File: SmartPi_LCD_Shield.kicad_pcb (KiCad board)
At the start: 2 copper layers, 84 x 58 mm, 47 parts, among them J1 Ant_SMA, J3 Micro_SD_Card, J4 Conn_01x02, J5 Conn_01x16, Q1 BC547, SW1 Reset, SW2 UP, SW3 LEFT, SW4 RIGHT, SW5 SELECT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

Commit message: finished routing
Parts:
- added CreativeCommonsPublicDomain1: License, Symbol:Symbol_CreativeCommonsPublicDomain_SilkScreenTop_Small, B.Cu at (182.9, 123.8)
- added J2: Conn_01x01, Connector_PinSocket_2.54mm:PinSocket_1x01_P2.54mm_Vertical, F.Cu at (225.4, 127.0)
- added KiCad1: License, Symbol:KiCad-Logo2_8mm_SilkScreen, B.Cu at (184.8, 113.7)
- added RV2: 10k, Potentiometer_THT:Potentiometer_Bourns_3296X_Horizontal, F.Cu at (153.0, 98.4)
- JP6: moved to F.Cu
- LOGO1: footprint Symbol:OSHW-Logo2_7.3x6mm_SilkScreen -> Symbol:OSHW-Logo2_14.6x12mm_SilkScreen; moved to B.Cu
- moved LOGO1 88.6 mm to (170.8, 112.4)
- moved JP6 57.8 mm to (221.0, 97.8), turned to 270 degrees
- moved JP14 43.0 mm to (208.3, 140.3), turned to 180 degrees
- moved JP1 27.1 mm to (171.4, 97.8), turned to 90 degrees
- moved TP4 4.84 mm to (210.2, 132.1)
- moved TP2 4.62 mm to (218.4, 132.1)
- moved TP5 4.49 mm to (213.4, 132.1)
- moved TP3 4.44 mm to (221.6, 132.1)
- moved J3 2.54 mm to (219.7, 113.7)
- moved JP10 2.54 mm to (165.1, 131.4)
- moved JP11 2.54 mm to (162.6, 131.4)
- moved JP9 2.54 mm to (167.6, 131.4)
- moved TP6 2.54 mm to (200.0, 120.7)
- moved TP1 2.29 mm to (219.7, 107.3)
- moved RV1 1.91 mm to (153.0, 93.3)
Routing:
- net Net-(JP6-Pad2): track 3.16 -> 132.8 mm
- net Net-(BT1-Pad1): track 0.00 -> 110.9 mm
- net +5V: track 57.8 -> 143.9 mm
- net /SCL: track 63.4 -> 134.9 mm
- net /SDA: track 68.2 -> 136.2 mm
- net +3V3: track 96.7 -> 163.6 mm
- net Net-(JP12-Pad2): track 12.1 -> 77.7 mm
- net /RFM_D0: track 3.16 -> 64.2 mm
- net /CLK: track 9.26 -> 56.9 mm
- net /Key0: track 37.7 -> 46.1 mm
- net /RW: track 25.1 -> 32.3 mm
- net GND: track 0.00 -> 6.99 mm, vias 0 -> 55
- net /MISO: track 41.7 -> 48.0 mm
- net /SS2: track 34.0 -> 28.0 mm
- net Net-(A1-Pad3): track 124.4 -> 129.4 mm
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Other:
- net class PWR added: clearance 0, trace_width 0.5, via_dia 0.8, via_drill 0.4
- net class sat added: clearance 0.5, trace_width 1, via_dia 0.8, via_drill 0.4
- board text added: "SmartPi LCD Shield"
- board text added: "https://github.com/nerdyscout/SmartPi_LCD_Shield"

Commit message: added hexbuffer for sd card
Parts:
- added TP7: TestPoint, TestPoint:TestPoint_Pad_D1.5mm, F.Cu at (256.5, 109.2)
- added TP8: TestPoint, TestPoint:TestPoint_Pad_D1.5mm, F.Cu at (254.6, 105.4)
- added U4: 4050, Package_SO:SOIC-16_3.9x9.9mm_P1.27mm, F.Cu at (208.3, 127.0)
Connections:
- BZ1 pad 1: +5V -> (no net)
- J3 pad 2: /SS3 -> Net-(J3-Pad2)
- J3 pad 5: /CLK -> Net-(J3-Pad5)
- J3 pad 7: /MISO -> Net-(J3-Pad7)
- JP10 pad 3: +3V3 -> +5V
- JP11 pad 3: +3V3 -> +5V
- JP9 pad 3: +3V3 -> +5V
- R1 pad 2: +3V3 -> +5V
- R2 pad 2: +3V3 -> +5V
- R3 pad 2: +3V3 -> +5V
- R4 pad 2: +3V3 -> +5V
- U2 pad 18: +3V3 -> +5V
- U2 pad 9: +3V3 -> +5V
- U3 pad 2: +3V3 -> +5V
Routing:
- net /SS3: track 50.6 -> 0.00 mm
- net /MOSI: track 47.4 -> 28.4 mm, vias 1 -> 0
- net /MISO: track 48.0 -> 29.4 mm, vias 1 -> 0
- net /CLK: track 56.9 -> 39.3 mm, vias 1 -> 0
- net GND: vias 55 -> 54
- net /SCL: vias 0 -> 1

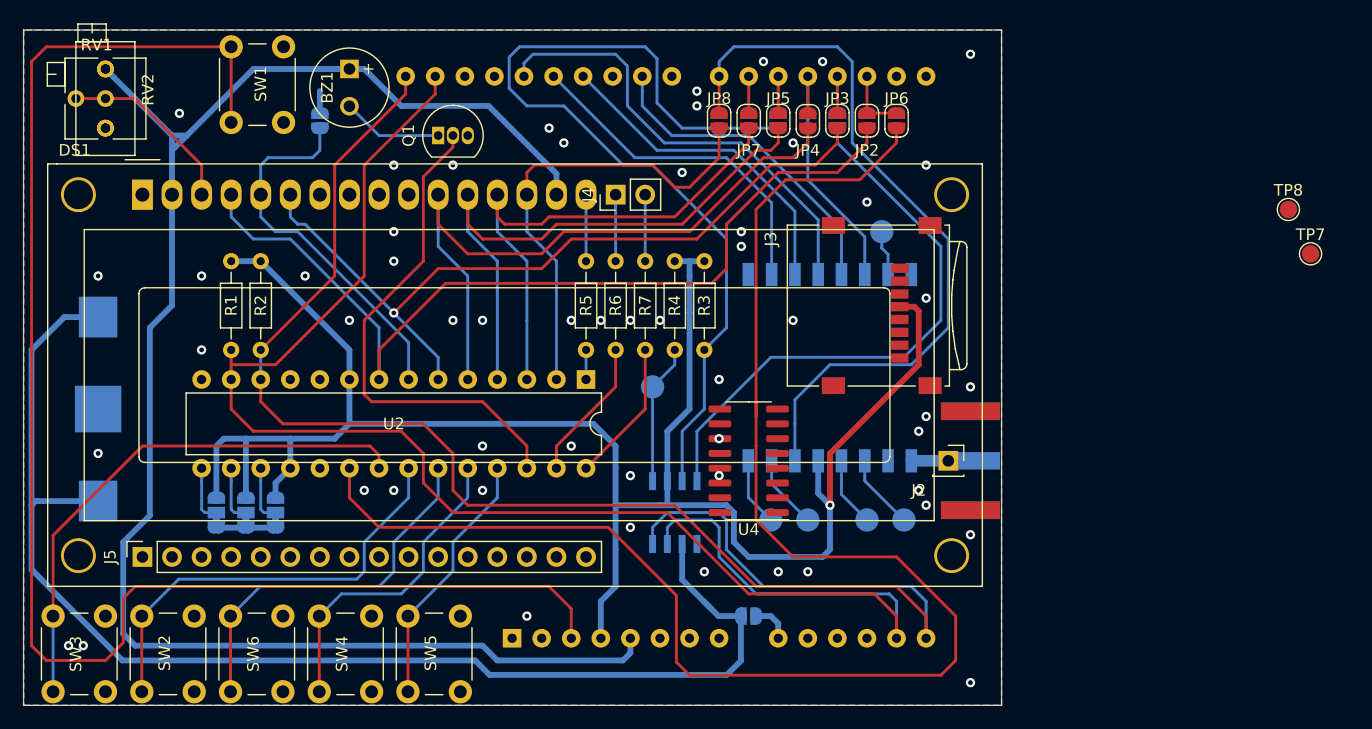
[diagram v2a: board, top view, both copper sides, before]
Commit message: routing complete with hex buffer
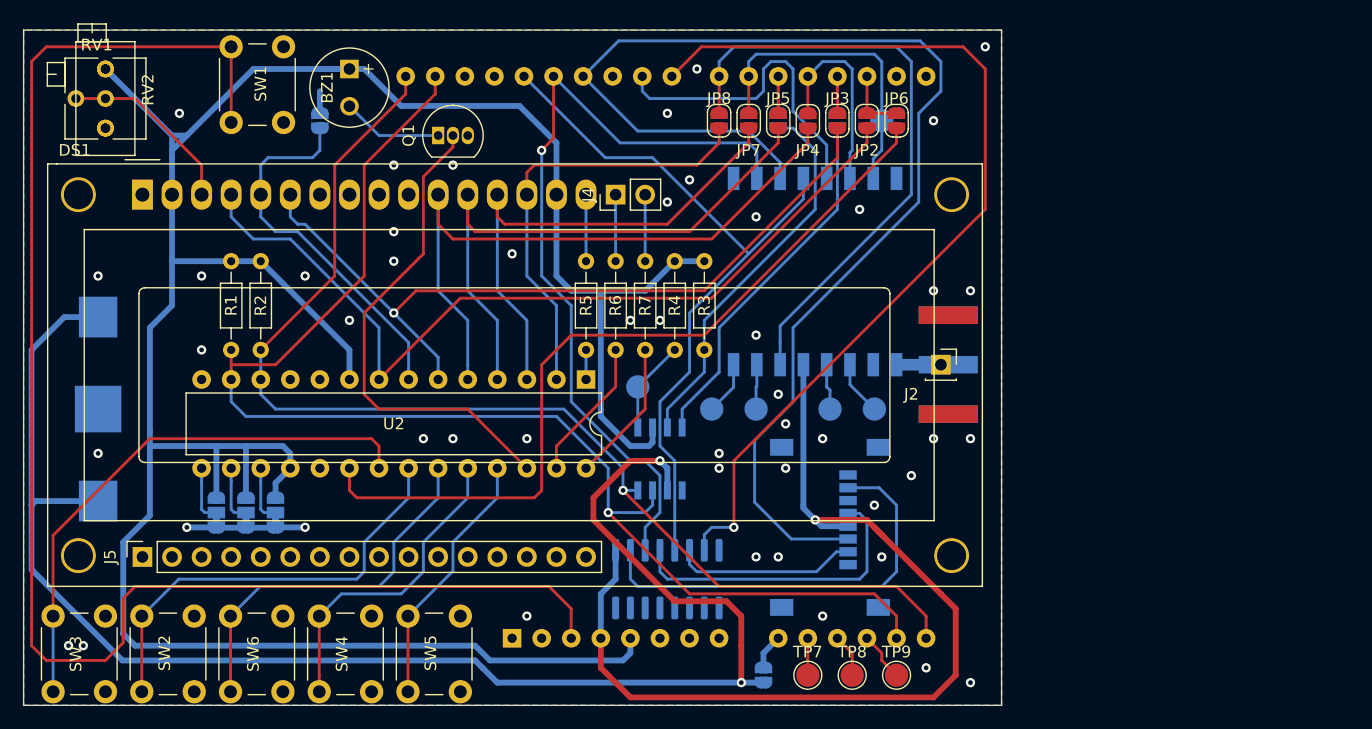
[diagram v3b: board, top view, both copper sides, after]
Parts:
- removed CreativeCommonsPublicDomain1: License, Symbol:Symbol_CreativeCommonsPublicDomain_SilkScreenTop_Small
- added TP9: TestPoint, TestPoint:TestPoint_Pad_D2.0mm, F.Cu at (221.0, 145.4)
- J3, U4: moved to B.Cu
- TP7, TP8: footprint TestPoint:TestPoint_Pad_D1.5mm -> TestPoint:TestPoint_Pad_D2.0mm
- moved TP7 56.3 mm to (213.4, 145.4)
- moved TP8 54.8 mm to (217.2, 145.4)
- moved J3 19.6 mm to (215.3, 132.7), turned to 90 degrees
- moved U4 12.3 mm to (201.3, 137.2), turned to 270 degrees
- moved TP4 10.8 mm to (205.1, 122.6)
- moved TP5 10.5 mm to (208.9, 122.6)
- moved TP2 10.0 mm to (215.3, 122.6)
- moved TP3 9.86 mm to (219.1, 122.6)
- moved TP1 9.52 mm to (219.7, 97.8)
- moved J1 8.47 mm to (225.4, 118.7)
- moved U1 8.35 mm to (214.0, 110.7)
- moved J2 8.28 mm to (224.8, 118.7)
- moved JP14 5.23 mm to (209.6, 145.4), turned to 270 degrees
- moved U3 4.78 mm to (200.7, 126.8)
- moved TP6 1.27 mm to (198.8, 120.7)
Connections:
- net Net-(TP4-Pad1) renamed /RFM_D2
- net Net-(TP5-Pad1) renamed /RFM_D1
- A1 pad 10: (no net) -> Net-(A1-Pad10)
- A1 pad 11: (no net) -> Net-(A1-Pad11)
- A1 pad 12: (no net) -> Net-(A1-Pad12)
- A1 pad 21: Net-(A1-Pad21) -> /RFM_D5
- BZ1 pad 1: (no net) -> +5V
- JP7 pad 2: Net-(A1-Pad21) -> /RFM_D5
- TP1 pad 1: Net-(TP1-Pad1) -> /RFM_D5
- TP7 pad 1: Net-(TP?1558479045-Pad1) -> Net-(A1-Pad10)
- TP8 pad 1: Net-(TP?1558480511-Pad1) -> Net-(A1-Pad11)
- U1 pad 7: Net-(TP1-Pad1) -> /RFM_D5
- U4 pad 10: Net-(TP?1558479045-Pad1) -> (no net)
- U4 pad 11: /SCL -> (no net)
- U4 pad 12: Net-(TP?1558480511-Pad1) -> (no net)
- U4 pad 2: Net-(J3-Pad2) -> Net-(J3-Pad7)
- U4 pad 3: /SS3 -> /MISO
- U4 pad 6: Net-(J3-Pad7) -> Net-(J3-Pad2)
- U4 pad 7: /MISO -> /SS3
- U4 pad 9: /SDA -> (no net)
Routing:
- net +5V: track 143.9 -> 230.8 mm
- net +3V3: track 163.6 -> 81.6 mm
- net /SS3: track 0.00 -> 81.2 mm, vias 0 -> 1
- net /MOSI: track 28.4 -> 107.9 mm
- net Net-(JP6-Pad2): track 132.8 -> 69.4 mm
- net Net-(JP12-Pad2): track 77.7 -> 33.0 mm
- net /MISO: track 29.4 -> 69.1 mm, vias 0 -> 1
- net Net-(J3-Pad7): track 0.00 -> 36.6 mm
- net /SCL: track 134.9 -> 101.8 mm
- net /RFM_D5: track 0.00 -> 26.7 mm
- net Net-(J3-Pad5): track 0.00 -> 26.4 mm
- net /CLK: track 39.3 -> 63.2 mm
- net /SDA: track 136.2 -> 113.0 mm, vias 0 -> 1
- net Net-(BT1-Pad1): track 110.9 -> 132.1 mm, vias 0 -> 2
- net Net-(JP13-Pad1): track 49.5 -> 31.2 mm
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
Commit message: added option for analog buttons
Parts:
- removed TP7: TestPoint, TestPoint:TestPoint_Pad_D2.0mm
- added R10: 620, Resistor_THT:R_Axial_DIN0204_L3.6mm_D1.6mm_P7.62mm_Horizontal, F.Cu at (172.7, 130.2)
- added R11: 1k, Resistor_THT:R_Axial_DIN0204_L3.6mm_D1.6mm_P7.62mm_Horizontal, F.Cu at (163.8, 137.8)
- added R12: 3k3, Resistor_THT:R_Axial_DIN0204_L3.6mm_D1.6mm_P7.62mm_Horizontal, F.Cu at (180.3, 132.7)
- added R8: 2k, Resistor_THT:R_Axial_DIN0204_L3.6mm_D1.6mm_P7.62mm_Horizontal, F.Cu at (186.7, 137.8)
- added R9: 330, Resistor_THT:R_Axial_DIN0204_L3.6mm_D1.6mm_P7.62mm_Horizontal, F.Cu at (148.6, 137.8)
- moved SW2 0.06 mm to (160.7, 140.3)
- moved SW3 0.06 mm to (153.1, 140.3)
- moved SW5 0.06 mm to (183.6, 140.3)
- moved SW6 0.06 mm to (168.3, 140.3)
- moved SW4 0.05 mm to (175.9, 140.3)
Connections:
- A1 pad 10: Net-(A1-Pad10) -> /A1
- SW5 pad 2: /Key4 -> /A1
- U2 pad 25: /Key4 -> /A1
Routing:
- net /A1: track 0.00 -> 67.1 mm
- net /Key4: track 22.4 -> 0.00 mm
- net Net-(A1-Pad3): track 129.4 -> 120.9 mm
- net +5V: track 230.8 -> 237.1 mm
- net /Key2: track 32.6 -> 37.4 mm
- net Net-(A1-Pad10): track 3.17 -> 0.00 mm
- net Net-(JP6-Pad2): track 69.4 -> 67.2 mm
- net /Key3: track 27.5 -> 29.3 mm
- net /Key1: track 37.7 -> 39.5 mm
- net /Key0: track 47.0 -> 45.7 mm
- net /RS: track 74.6 -> 75.3 mm
- net GND: vias 49 -> 47
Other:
- board text added: "beta"
